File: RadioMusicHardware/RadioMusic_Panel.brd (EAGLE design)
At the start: 128.5 x 20 mm, 13 parts, among them X1 VERT_SD_CARD

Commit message: Panel design
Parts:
- removed CHANNEL-CV, OUTPUT, RESET-CV, TIME-CV: (no value), thonkiconn:WQP-PJ301M-12_JACK
- removed CHANNEL-POT, TIME-POT: 50k, TomW:EVUF
- removed LED1, LED2, LED3, LED4, LED5: (no value), TomW:LED3MM
- removed RESET: D6_PUSH_SWITCH, TomW:D6_BUTTON_RND
- removed X1: VERT_SD_CARD, TomW:VERT_MICROSD
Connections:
- removed net +3.3V_F: TIME-POT.3
- removed net GND_F: CHANNEL-CV.P$3
- removed net LED3_F: LED3.A
- removed net LED4_F: LED4.A
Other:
- outline, holes or cut-outs redrawn
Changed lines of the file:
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@@
 <setting verticaltext="up"/>
 </settings>
-<grid distance="25" unitdist="mil" unit="mm" style="lines" multiple="1" display="yes" altdistance="8" altunitdist="mil" altunit="mil"/>
+<grid distance="25" unitdist="mil" unit="mm" style="lines" multiple="1" display="yes" altdistance="0.1" altunitdist="mm" altunit="mm"/>
 <layers>
 <layer number="1" name="Top" color="4" fill="1" visible="yes" active="yes"/>
@@
 <wire x1="128.5" y1="0" x2="128.5" y2="20" width="0.0254" layer="20"/>
 <wire x1="128.5" y1="20" x2="0" y2="20" width="0.0254" layer="20"/>
-<wire x1="130.75" y1="10" x2="-9.25" y2="10" width="0.1" layer="51"/>
-<wire x1="64.25" y1="-9.5" x2="64.25" y2="30.5" width="0.1" layer="51"/>
+<rectangle x1="48.1" y1="14" x2="61.6" y2="16.8" layer="46"/>
+<hole x="63.455" y="3.675" drill="3.1"/>
+<hole x="115.906" y="16.756" drill="3.1"/>
+<hole x="115.906" y="12.311" drill="3.1"/>
+<hole x="115.906" y="7.866" drill="3.1"/>
+<hole x="115.906" y="3.421" drill="3.1"/>
 </plain>
 <attributes>
@@
 </autorouter>
 <elements>
-<element name="CHANNEL-POT" library="TomW" package="EVUF" value="50k" x="106" y="10.025" smashed="yes" rot="R270">
-<attribute name="NAME" x="108.825" y="13.66" size="0.6096" layer="25" rot="R270"/>
-<attribute name="VALUE" x="101.58" y="11.985" size="0.6096" layer="27" rot="R270"/>
-</element>
-<element name="CHANNEL-CV" library="thonkiconn" package="WQP-PJ301M-12_JACK" value="" x="31.705" y="5.58" rot="R90"/>
-<element name="RESET-CV" library="thonkiconn" package="WQP-PJ301M-12_JACK" value="" x="17.1" y="15.105" rot="R90"/>
-<element name="OUTPUT" library="thonkiconn" package="WQP-PJ301M-12_JACK" value="" x="17.1" y="4.945" rot="R90"/>
-<element name="TIME-POT" library="TomW" package="EVUF" value="50k" x="78.06" y="10.025" smashed="yes" rot="R270">
-<attribute name="NAME" x="80.6" y="13.835" size="0.6096" layer="25" rot="R270"/>
-<attribute name="VALUE" x="74.25" y="13.835" size="0.6096" layer="27" rot="R270"/>
-</element>
-<element name="TIME-CV" library="thonkiconn" package="WQP-PJ301M-12_JACK" value="" x="31.705" y="15.105" rot="R90"/>
-<element name="RESET" library="TomW" package="D6_BUTTON_RND" value="D6_PUSH_SWITCH" x="55.2" y="6.85" rot="R180"/>
-<element name="LED1" library="TomW" package="LED3MM" value="" x="115.906" y="16.756" rot="R90"/>
-<element name="LED2" library="TomW" package="LED3MM" value="" x="115.906" y="12.311" rot="R90"/>
-<element name="LED3" library="TomW" package="LED3MM" value="" x="115.906" y="7.866" rot="R270"/>
-<element name="LED4" library="TomW" package="LED3MM" value="" x="115.906" y="3.421" rot="R270"/>
-<element name="X1" library="TomW" package="VERT_MICROSD" value="VERT_SD_CARD" x="55.2" y="17.01"/>
-<element name="LED5" library="TomW" package="LED3MM" value="" x="63.455" y="3.675" rot="R270"/>
 </elements>
 <signals>
 <signal name="VBAT">
 </signal>
-<signal name="LED4_F">
-<contactref element="LED4" pad="A"/>
-</signal>
-<signal name="LED3_F">
-<contactref element="LED3" pad="A"/>
-</signal>
-<signal name="+3.3V_F">
-<contactref element="TIME-POT" pad="3"/>
-</signal>
-<signal name="GND_F" class="2" airwireshidden="yes">
-<contactref element="CHANNEL-CV" pad="P$3"/>
-</signal>
-<signal name="N$1">
+<signal name="GND">
+<via x="17.1" y="15.105" extent="1-16" drill="6"/>
+<via x="31.705" y="15.105" extent="1-16" drill="6"/>
+<via x="17.1" y="4.945" extent="1-16" drill="6"/>
+<via x="31.705" y="4.945" extent="1-16" drill="6"/>
+<via x="55.2" y="6.85" extent="1-16" drill="9.2"/>
+<via x="78.06" y="10.025" extent="1-16" drill="7.1"/>
 <via x="3" y="12.5" extent="1-16" drill="3.2"/>
-</signal>
-<signal name="N$2">
+<via x="106" y="10.025" extent="1-16" drill="7.1"/>
 <via x="125.5" y="12.5" extent="1-16" drill="3.2"/>
+<wire x1="106" y1="10.025" x2="125.5" y2="12.5" width="0" layer="19" extent="1-1"/>
+<wire x1="78.06" y1="10.025" x2="106" y2="10.025" width="0" layer="19" extent="1-1"/>
+<wire x1="55.2" y1="6.85" x2="78.06" y2="10.025" width="0" layer="19" extent="1-1"/>
+<wire x1="31.705" y1="4.945" x2="55.2" y2="6.85" width="0" layer="19" extent="1-1"/>
+<wire x1="31.705" y1="15.105" x2="31.705" y2="4.945" width="0" layer="19" extent="1-1"/>
+<wire x1="17.1" y1="15.105" x2="31.705" y2="15.105" width="0" layer="19" extent="1-1"/>
+<wire x1="17.1" y1="4.945" x2="17.1" y2="15.105" width="0" layer="19" extent="1-1"/>
+<wire x1="3" y1="12.5" x2="17.1" y2="15.105" width="0" layer="19" extent="1-1"/>
 </signal>
 </signals>

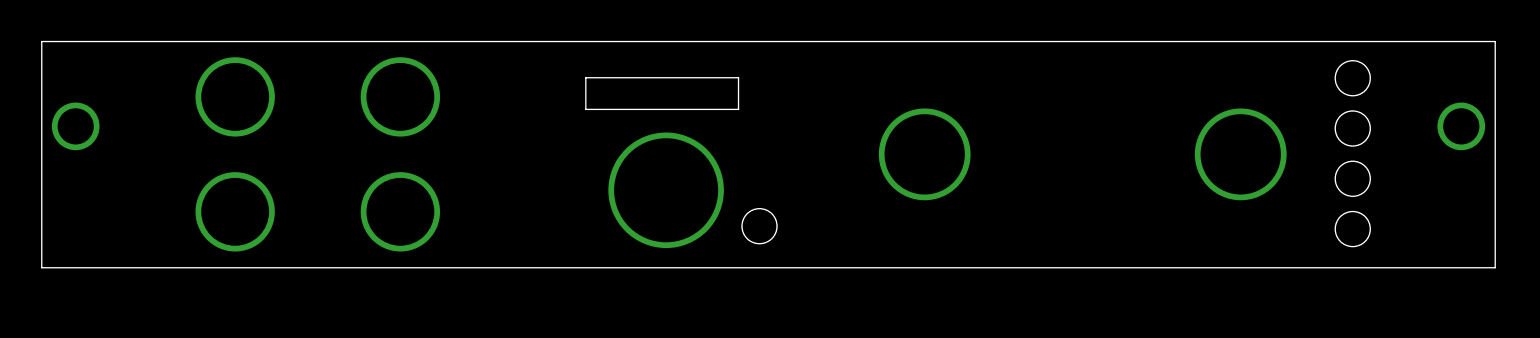
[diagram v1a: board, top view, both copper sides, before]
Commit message: Artwork on panels, notes on PCBs
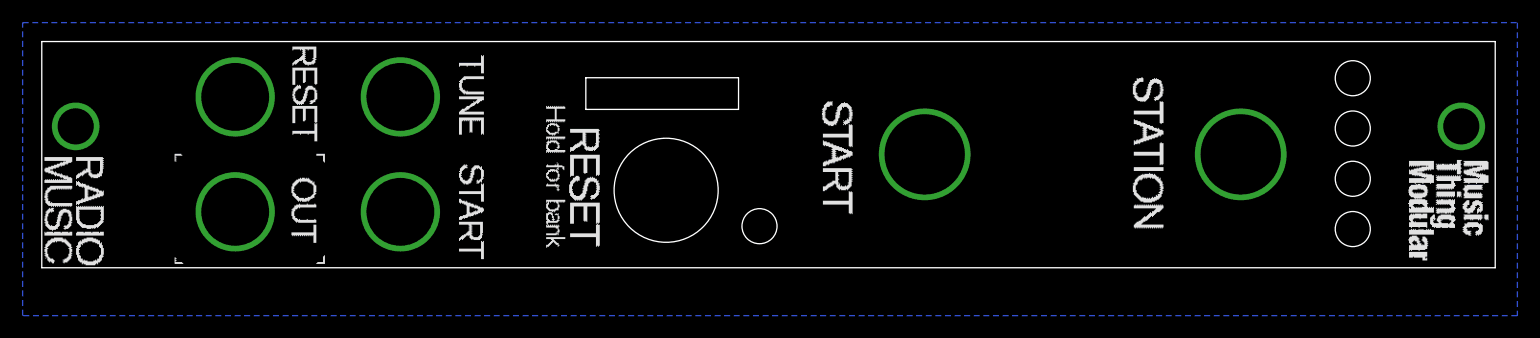
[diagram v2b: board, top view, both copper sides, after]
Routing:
- added copper zone on layer 16, net GND
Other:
- board text added: "RadioMusic Panel PCB rev 1 Designed in Herne Hill, London by Tom Whitwell October 2014 CC-BY-SA musicthing.co.uk"
